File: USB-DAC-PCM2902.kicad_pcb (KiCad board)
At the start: 2 copper layers, 61 x 34.8 mm, 32 parts, among them J1 Conn_01x02, J2 PJ-320D, SW1 MUTE, SW2 VOL_DOWN, SW3 VOL_UP, U1 USB_PCB, U2 PCM2902, U3 LP2951CM, Y1 O12M

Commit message: upadte pcb shape,
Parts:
- moved J1 11.9 mm to (60.3, 2.04), turned to 0 degrees
- moved R1 8.90 mm to (21.1, 3.00)
- moved R7 4.68 mm to (23.4, 23.5), turned to 180 degrees
- moved R3 3.12 mm to (17.0, 14.8)
- moved D1 2.12 mm to (14.1, 6.78)
- moved R4 2.12 mm to (18.7, 6.82)
- moved C1 2.00 mm to (55.0, 14.7)
- moved C10 2.00 mm to (24.7, 28.6)
- moved C11 2.00 mm to (36.6, 28.0)
- moved C2 2.00 mm to (46.6, 14.5)
- moved C3 2.00 mm to (55.8, 2.49)
- moved C4 2.00 mm to (46.6, 20.1)
- moved C5 2.00 mm to (48.3, 2.49)
- moved C6 2.00 mm to (55.0, 20.1)
- moved C7 2.00 mm to (24.6, 26.7)
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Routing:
- net GND: track 162.8 -> 173.0 mm
- net Net-(C7-Pad1): track 41.9 -> 31.8 mm
- net Net-(C1-Pad1): track 64.3 -> 74.3 mm
- net Net-(J1-Pad2): track 25.3 -> 33.0 mm
- net /VOL_DOWN: track 32.5 -> 38.8 mm
- net Net-(R4-Pad2): track 57.5 -> 63.1 mm
- net Net-(C2-Pad1): track 13.5 -> 8.06 mm, vias 2 -> 0
- net /VOL_UP: track 27.4 -> 32.7 mm
- net Net-(C3-Pad2): track 38.8 -> 33.8 mm
- net /VOL_MUTE: track 40.4 -> 44.9 mm
- net Net-(C7-Pad2): track 11.2 -> 7.50 mm
- net Net-(C5-Pad2): track 36.1 -> 32.6 mm
- net Net-(R3-Pad2): track 8.59 -> 12.0 mm
- net Net-(C10-Pad1): track 12.2 -> 9.88 mm
- net Net-(C6-Pad1): track 26.6 -> 28.3 mm
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- added copper zone on B.Cu, net GND
- added copper zone on F.Cu, net GND
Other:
- board size 61 x 34.8 mm -> 63 x 34.8 mm
- net class Default: trace_width 0.25 -> 0.4

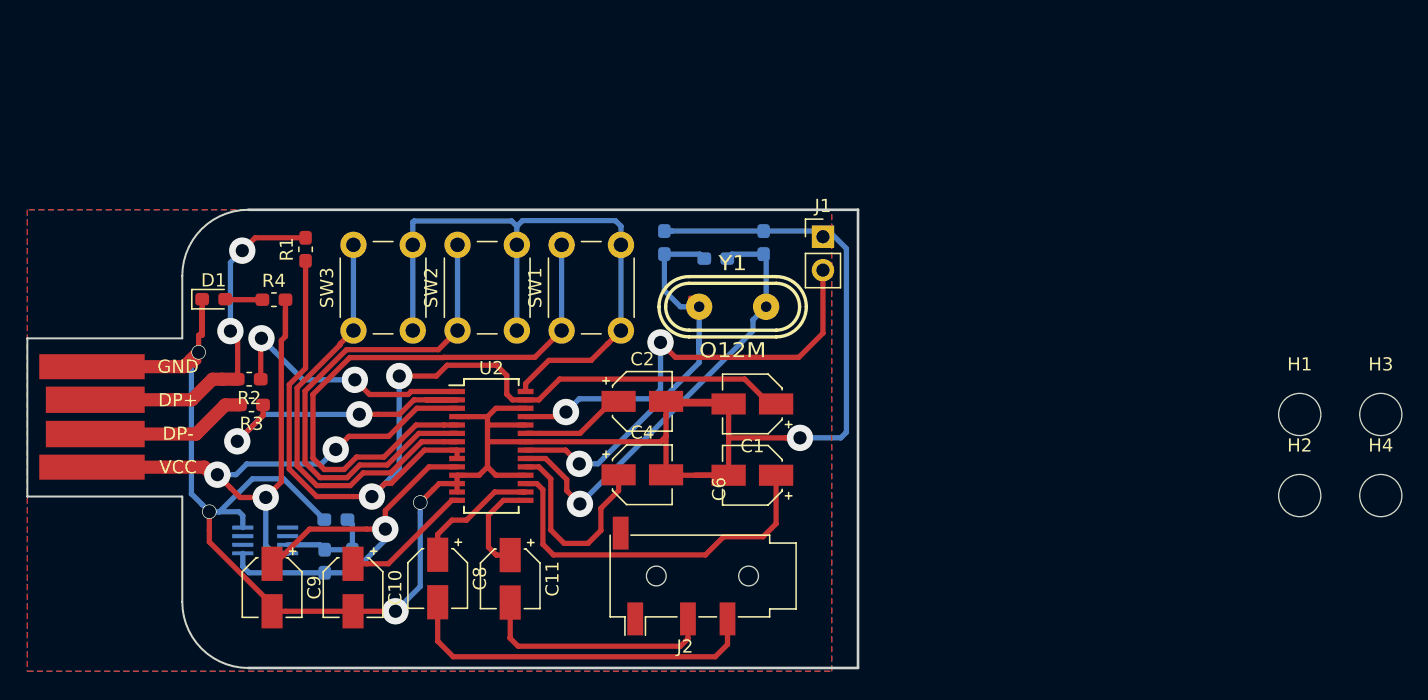
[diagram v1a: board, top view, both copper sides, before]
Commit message: upadte pcb shape,
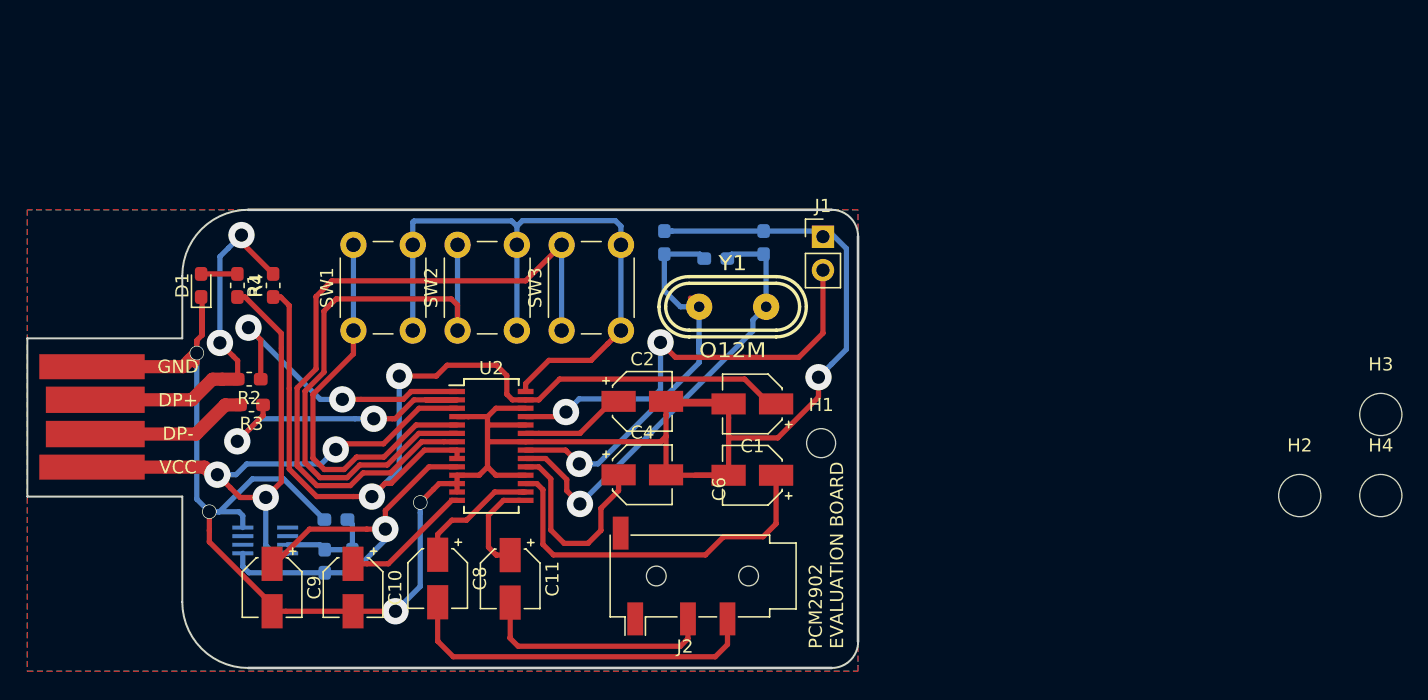
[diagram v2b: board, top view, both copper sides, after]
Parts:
- H1: footprint MountingHole:MountingHole_3.2mm_M3_DIN965 -> MountingHole:MountingHole_2.2mm_M2_DIN965
- moved H1 36.4 mm to (60.2, 17.7)
- moved SW1 15.8 mm to (24.7, 9.16)
- moved SW3 15.8 mm to (40.5, 9.16)
- moved R1 3.68 mm to (18.6, 5.74)
- moved R4 2.97 mm to (15.9, 5.74), turned to 270 degrees
- moved D1 1.41 mm to (13.2, 5.74), turned to 90 degrees
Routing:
- net /VOL_UP: track 32.7 -> 54.3 mm
- net /VOL_MUTE: track 44.9 -> 30.1 mm
- net /VOL_DOWN: track 38.8 -> 44.6 mm
- net GND: track 173.0 -> 169.5 mm
- net Net-(R2-Pad1): track 19.8 -> 22.6 mm
- net Net-(C1-Pad1): track 74.3 -> 71.9 mm
- net Net-(R1-Pad2): track 27.0 -> 27.6 mm
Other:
- outline, holes or cut-outs redrawn
- board text added: "PCM2902 EVALUATION BOARD"

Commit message: update,
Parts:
- C3, C5, R5: moved to F.Cu
- H2, H3, H4: footprint MountingHole:MountingHole_3.2mm_M3_DIN965 -> MountingHole:MountingHole_2.2mm_M2_DIN965
- J2: footprint Connector_Audio:Jack_3.5mm_PJ320D_Horizontal -> footprint-lib:PJ320D_3.5mm_Jack
- Y1: footprint w_crystal:crystal_hc-49s -> Crystal:Crystal_SMD_HC49-SD
- moved H4 83.7 mm to (19.5, 31.5)
- moved H2 81.1 mm to (17.5, 3.50)
- moved H3 64.5 mm to (43.4, -9.97)
- moved J1 38.1 mm to (22.2, 4.00)
- moved C1 6.00 mm to (49.0, 14.7)
- moved C2 6.00 mm to (40.6, 14.5)
- moved C4 6.00 mm to (40.6, 20.1)
- moved C6 6.00 mm to (49.0, 20.1)
- moved U2 6.00 mm to (29.2, 17.9)
- moved D1 5.71 mm to (15.4, 11.0)
- moved R1 5.71 mm to (20.9, 11.0)
- moved R4 5.71 mm to (18.2, 11.0)
- moved C10 3.75 mm to (22.4, 25.6)
- moved C9 3.75 mm to (16.3, 25.6)
- moved Y1 2.76 mm to (55.5, 9.25)
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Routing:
- net GND: track 169.5 -> 0.00 mm, vias 5 -> 0
- net Net-(C1-Pad1): track 71.9 -> 0.00 mm, vias 2 -> 0
- net Net-(R4-Pad2): track 62.8 -> 0.00 mm, vias 3 -> 0
- net /VOL_UP: track 54.3 -> 0.00 mm
- net /PIN28: track 49.9 -> 0.00 mm
- net /VOL_DOWN: track 44.6 -> 0.00 mm
- net Net-(C3-Pad2): track 33.8 -> 0.00 mm, vias 1 -> 0
- net Net-(J1-Pad2): track 33.0 -> 0.00 mm, vias 2 -> 0
- net Net-(C5-Pad2): track 32.6 -> 0.00 mm, vias 1 -> 0
- net Net-(C7-Pad1): track 31.8 -> 0.00 mm, vias 1 -> 0
- net /VOL_MUTE: track 30.1 -> 0.00 mm
- net Net-(C6-Pad1): track 28.3 -> 0.00 mm
- net /OUTL: track 27.8 -> 0.00 mm
- net Net-(R1-Pad2): track 27.6 -> 0.00 mm, vias 2 -> 0
- net Net-(R3-Pad1): track 23.9 -> 0.00 mm, vias 2 -> 0
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- removed copper zone on B.Cu, net GND
- removed copper zone on F.Cu, net GND
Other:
- net class Default: via_dia 0.8 -> 2.5; via_drill 0.4 -> 1

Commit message: update,
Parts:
- moved H3 48.6 mm to (68.5, 31.6)
- moved C9 8.89 mm to (24.2, 29.6)
- moved C10 8.83 mm to (30.4, 29.5)
- moved C11 6.33 mm to (42.5, 30.3)
- moved C8 6.33 mm to (37.0, 30.3)
- moved J2 4.03 mm to (54.0, 27.6)
- moved C7 3.83 mm to (22.2, 23.7)
- moved R6 3.83 mm to (20.1, 23.7)
- moved R7 3.59 mm to (21.1, 20.7)
- moved U3 2.81 mm to (15.9, 23.2)
- moved H1 2.02 mm to (59.4, 15.8)
- moved H4 2.00 mm to (17.5, 31.5)
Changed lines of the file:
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@@
   )
   (module MountingHole:MountingHole_2.2mm_M2_DIN965 (layer F.Cu)
-    (at 19.5 31.5)
+    (at 17.5 31.5)
     (descr "Mounting Hole 2.2mm, no annular, M2, DIN965")
     (tags "mounting hole 2.2mm no annular m2 din965")
@@
   )
   (module MountingHole:MountingHole_2.2mm_M2_DIN965 (layer F.Cu)
-    (at 43.4 -9.975)
+    (at 68.55 31.6)
     (descr "Mounting Hole 2.2mm, no annular, M2, DIN965")
     (tags "mounting hole 2.2mm no annular m2 din965")
@@
   )
   (module footprint-lib:PJ320D_3.5mm_Jack (layer F.Cu)
-    (at 49.925 27.775 180)
+    (at 53.95 27.55 180)
     (descr "Headphones with microphone connector, 3.5mm, 4 pins.")
     (tags "3.5mm jack mic microphone phones headphones 4pins audio plug")
@@
   )
   (module MountingHole:MountingHole_2.2mm_M2_DIN965 (layer F.Cu)
-    (at 60.2 17.7)
+    (at 59.4 15.85)
     (descr "Mounting Hole 2.2mm, no annular, M2, DIN965")
     (tags "mounting hole 2.2mm no annular m2 din965")
@@
   )
   (module Capacitor_SMD:CP_Elec_4x5.3 (layer F.Cu)
-    (at 31.12 27.965 270)
+    (at 37.02 30.265 270)
     (descr "SMT capacitor, aluminium electrolytic, 4x5.3, Vishay ")
     (tags "Capacitor Electrolytic")
@@
   )
   (module Capacitor_SMD:CP_Elec_4x5.3 (layer F.Cu)
-    (at 16.31 25.65 270)
+    (at 24.25 29.65 270)
     (descr "SMT capacitor, aluminium electrolytic, 4x5.3, Vishay ")
     (tags "Capacitor Electrolytic")
@@
   )
   (module Capacitor_SMD:CP_Elec_4x5.3 (layer F.Cu)
-    (at 22.45 25.65 270)
+    (at 30.4 29.5 270)
     (descr "SMT capacitor, aluminium electrolytic, 4x5.3, Vishay ")
     (tags "Capacitor Electrolytic")
@@
   )
   (module Capacitor_SMD:CP_Elec_4x5.3 (layer F.Cu)
-    (at 36.62 27.99 270)
+    (at 42.52 30.29 270)
     (descr "SMT capacitor, aluminium electrolytic, 4x5.3, Vishay ")
     (tags "Capacitor Electrolytic")
@@
   )
   (module Capacitor_SMD:C_0603_1608Metric_Pad1.05x0.95mm_HandSolder (layer B.Cu)
-    (at 24.65 26.655 90)
+    (at 22.2 23.705 90)
     (descr "Capacitor SMD 0603 (1608 Metric), square (rectangular) end terminal, IPC_7351 nominal with elongated pad for handsoldering. (Body size source: http://www.tortai-tech.com/upload/download/2011102023233369053.pdf), generated with kicad-footprint-generator")
     (tags "capacitor handsolder")
@@
   )
   (module Package_SO:SSOP-8_2.95x2.8mm_P0.65mm (layer B.Cu)
-    (at 18.04 25.08)
+    (at 15.95 23.2)
     (descr "SSOP-8 2.9 x2.8mm Pitch 0.65mm")
     (tags "SSOP-8 2.95x2.8mm Pitch 0.65mm")
@@
   )
   (module Resistor_SMD:R_0603_1608Metric_Pad1.05x0.95mm_HandSolder (layer B.Cu)
-    (at 22.55 26.655 90)
+    (at 20.1 23.705 90)
     (descr "Resistor SMD 0603 (1608 Metric), square (rectangular) end terminal, IPC_7351 nominal with elongated pad for handsoldering. (Body size source: http://www.tortai-tech.com/upload/download/2011102023233369053.pdf), generated with kicad-footprint-generator")
     (tags "resistor handsolder")
@@
   )
   (module Resistor_SMD:R_0603_1608Metric_Pad1.05x0.95mm_HandSolder (layer B.Cu)
-    (at 23.4 23.5 180)
+    (at 21.15 20.7 180)
     (descr "Resistor SMD 0603 (1608 Metric), square (rectangular) end terminal, IPC_7351 nominal with elongated pad for handsoldering. (Body size source: http://www.tortai-tech.com/upload/download/2011102023233369053.pdf), generated with kicad-footprint-generator")
     (tags "resistor handsolder")
